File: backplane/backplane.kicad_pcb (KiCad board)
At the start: 2 copper layers, 200 x 300 mm, 117 parts, among them J1 Conn_PCB1, J10 Conn_SSR_INPUT, J11 FAN, J12 Conn_SSR_PCB2, J13 FLOW, J14 FCC_B2B, J15 AQ2, J16 AQ1, J17 O3, J18 Conn_TO_ION_AIR, J2 Conn_PCB2, J22 POWER, J23 PCB1_COMM_CONNECTOR, J24 Conn_01x14, J25 PCB1_ALARM, J26 Conn_01x12, J27 Conn_01x15, J28 PMS7003S_CONN, J3 SSR_CONTROL, J4 TO_CONTROL_BOARD, J5 Conn_SSR_POWER_SOURCE, J6 48V_SRC, J7 WS2812, J8 PURFUME, J9 SSR2, Q1 2N3904(1AM), Q2 2N3904(1AM), Q3 2N3904(1AM), Q4 SS9013_J3, SW1 SW_Push, U1 OMRON-G3MB-202P, U2 OMRON-G3MB-202P, U3 waveshare-swd-pinsocket, U4 STM32F103C8T6, U5 AMS1117-3.3, U6 74AHCT1G125, U7 SP3232EEN, Y1 O8M, Y2 O_EPSON_32.768K

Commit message: update comments,
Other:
- board text added: "add 8 pin sub connector add mount hold for sub-board"
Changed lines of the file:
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@@
   (general
     (thickness 1.6)
-    (drawings 22)
+    (drawings 23)
     (tracks 1527)
     (zones 0)
@@
     )
   )
+  (gr_text "add 8 pin sub connector\nadd mount hold for sub-board\n" (at -5.21 44.15 90) (layer F.Cu)
+    (effects (font (size 1.5 1.5) (thickness 0.3)))
+  )
   (gr_circle (center 10 285) (end 16 285) (layer Dwgs.User) (width 1))

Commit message: update PCB2 done,
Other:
- board text added: "PCB2"

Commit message: update PCB1 done,
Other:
- board text added: "PCB1"
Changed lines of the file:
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@@
   (general
     (thickness 1.6)
-    (drawings 40)
+    (drawings 57)
     (tracks 1527)
     (zones 0)
@@
     )
   )
+  (gr_text PCB1 (at 335.5 245) (layer Dwgs.User)
+    (effects (font (size 3 3) (thickness 0.5)))
+  )
+  (gr_circle (center 321.75 202.25) (end 323.5 202.25) (layer Dwgs.User) (width 0.5))
+  (gr_circle (center 353.25 146.75) (end 355 146.75) (layer Dwgs.User) (width 0.5))
+  (gr_circle (center 353.25 202.25) (end 355 202.25) (layer Dwgs.User) (width 0.5))
+  (gr_circle (center 277.75 256.25) (end 279.5 256.25) (layer Dwgs.User) (width 0.5))
+  (gr_circle (center 341.75 256.25) (end 343.5 256.25) (layer Dwgs.User) (width 0.5))
+  (gr_circle (center 237.25 122.25) (end 239 122.25) (layer Dwgs.User) (width 0.5))
+  (gr_line (start 223.5 223.5) (end 223.5 118.5) (layer Dwgs.User) (width 0.5))
+  (gr_line (start 203.5 223) (end 223.5 223) (layer Dwgs.User) (width 0.5))
+  (gr_line (start 203.5 263) (end 203.5 223) (layer Dwgs.User) (width 0.5))
+  (gr_line (start 348.5 263) (end 203.5 263) (layer Dwgs.User) (width 0.5))
+  (gr_line (start 348.5 221) (end 348.5 263) (layer Dwgs.User) (width 0.5))
+  (gr_line (start 358 221) (end 348.5 221) (layer Dwgs.User) (width 0.5))
+  (gr_line (start 358 131) (end 358 221) (layer Dwgs.User) (width 0.5))
+  (gr_line (start 348 131) (end 358 131) (layer Dwgs.User) (width 0.5))
+  (gr_line (start 348 118.5) (end 348 131) (layer Dwgs.User) (width 0.5))
+  (gr_line (start 223.5 118.5) (end 348 118.5) (layer Dwgs.User) (width 0.5))
   (gr_circle (center 392.25 111.25) (end 394 111.25) (layer Dwgs.User) (width 0.5))
   (gr_circle (center 308.75 111.25) (end 310.5 111.25) (layer Dwgs.User) (width 0.5))

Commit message: align mounting hole,
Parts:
- H1, H16, H2, H3, H4, H5, H6, H7, H8, H9: footprint MountingHole:MountingHole_3.2mm_M3_DIN965 -> MountingHole:MountingHole_3.7mm
- moved H3 22.5 mm to (195.8, 150.2)
- moved H1 1.41 mm to (79.8, 125.8)
- moved H5 1.12 mm to (195.8, 205.8)
- moved H4 0.90 mm to (105.8, 107.8)
- moved H2 0.75 mm to (189.2, 107.8)
- moved H8 0.56 mm to (105.8, 6.75)
- moved H6 0.25 mm to (189.2, 6.75)

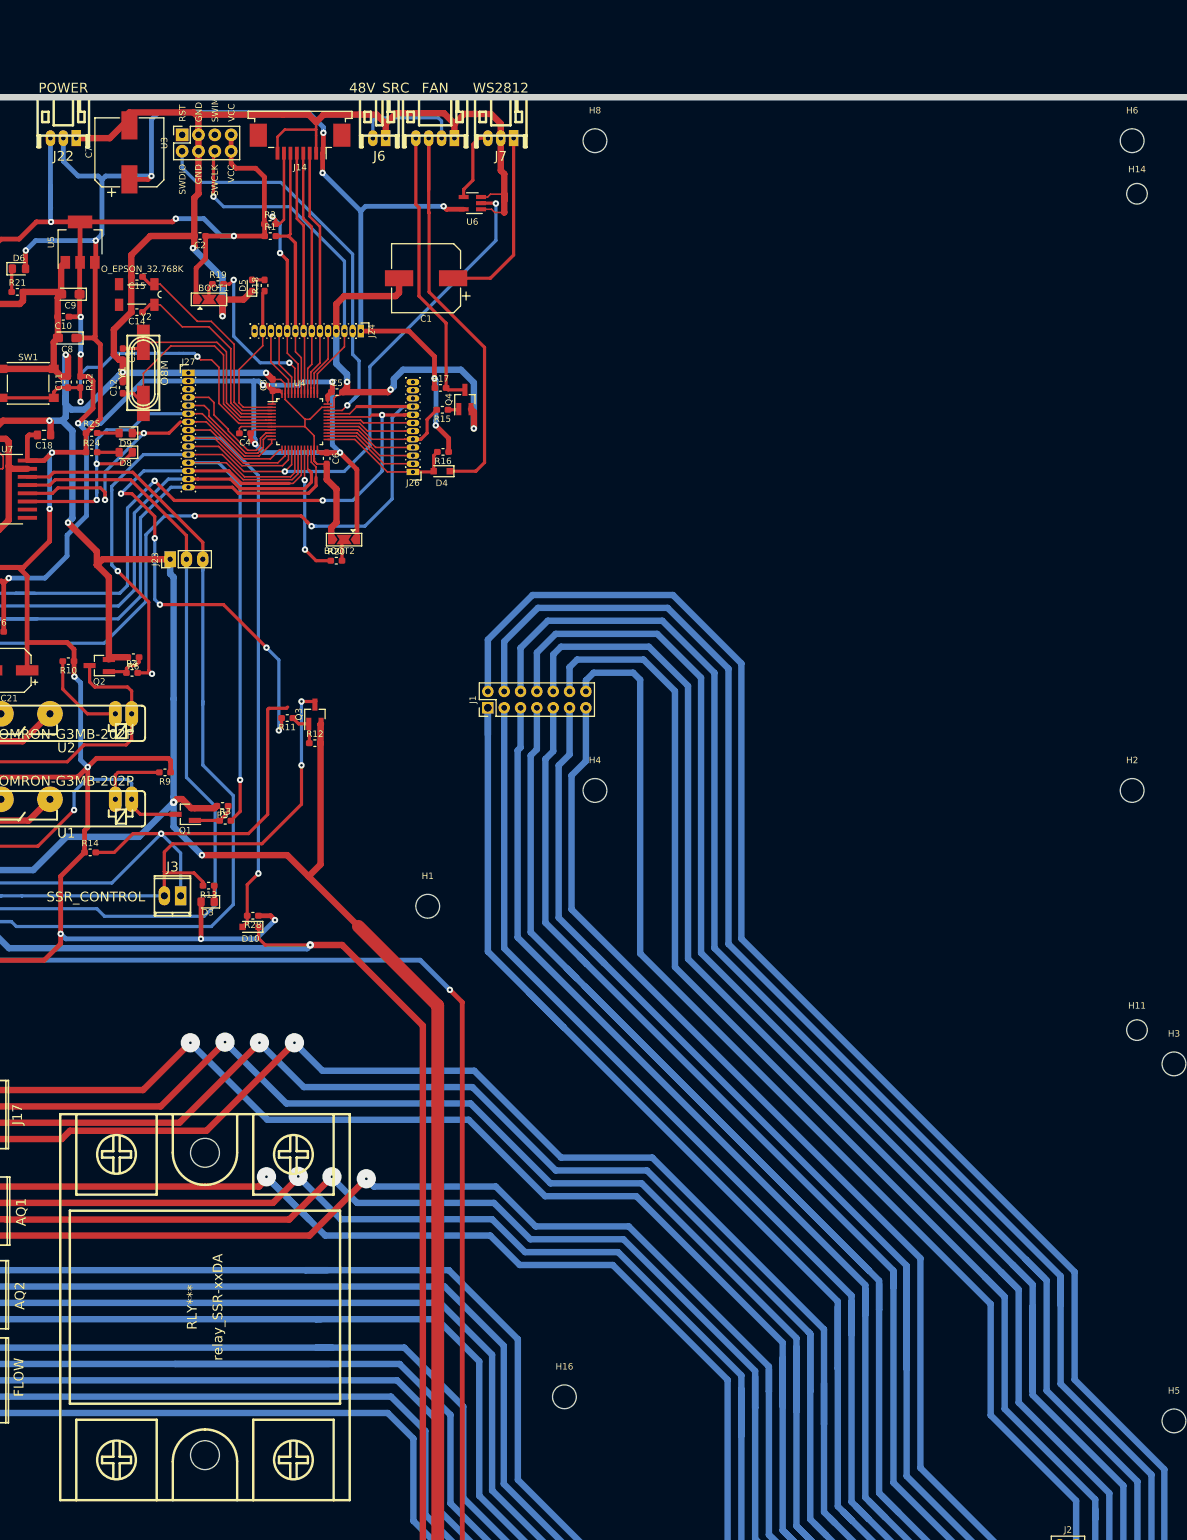
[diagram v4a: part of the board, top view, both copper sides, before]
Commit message: align mounting hole,
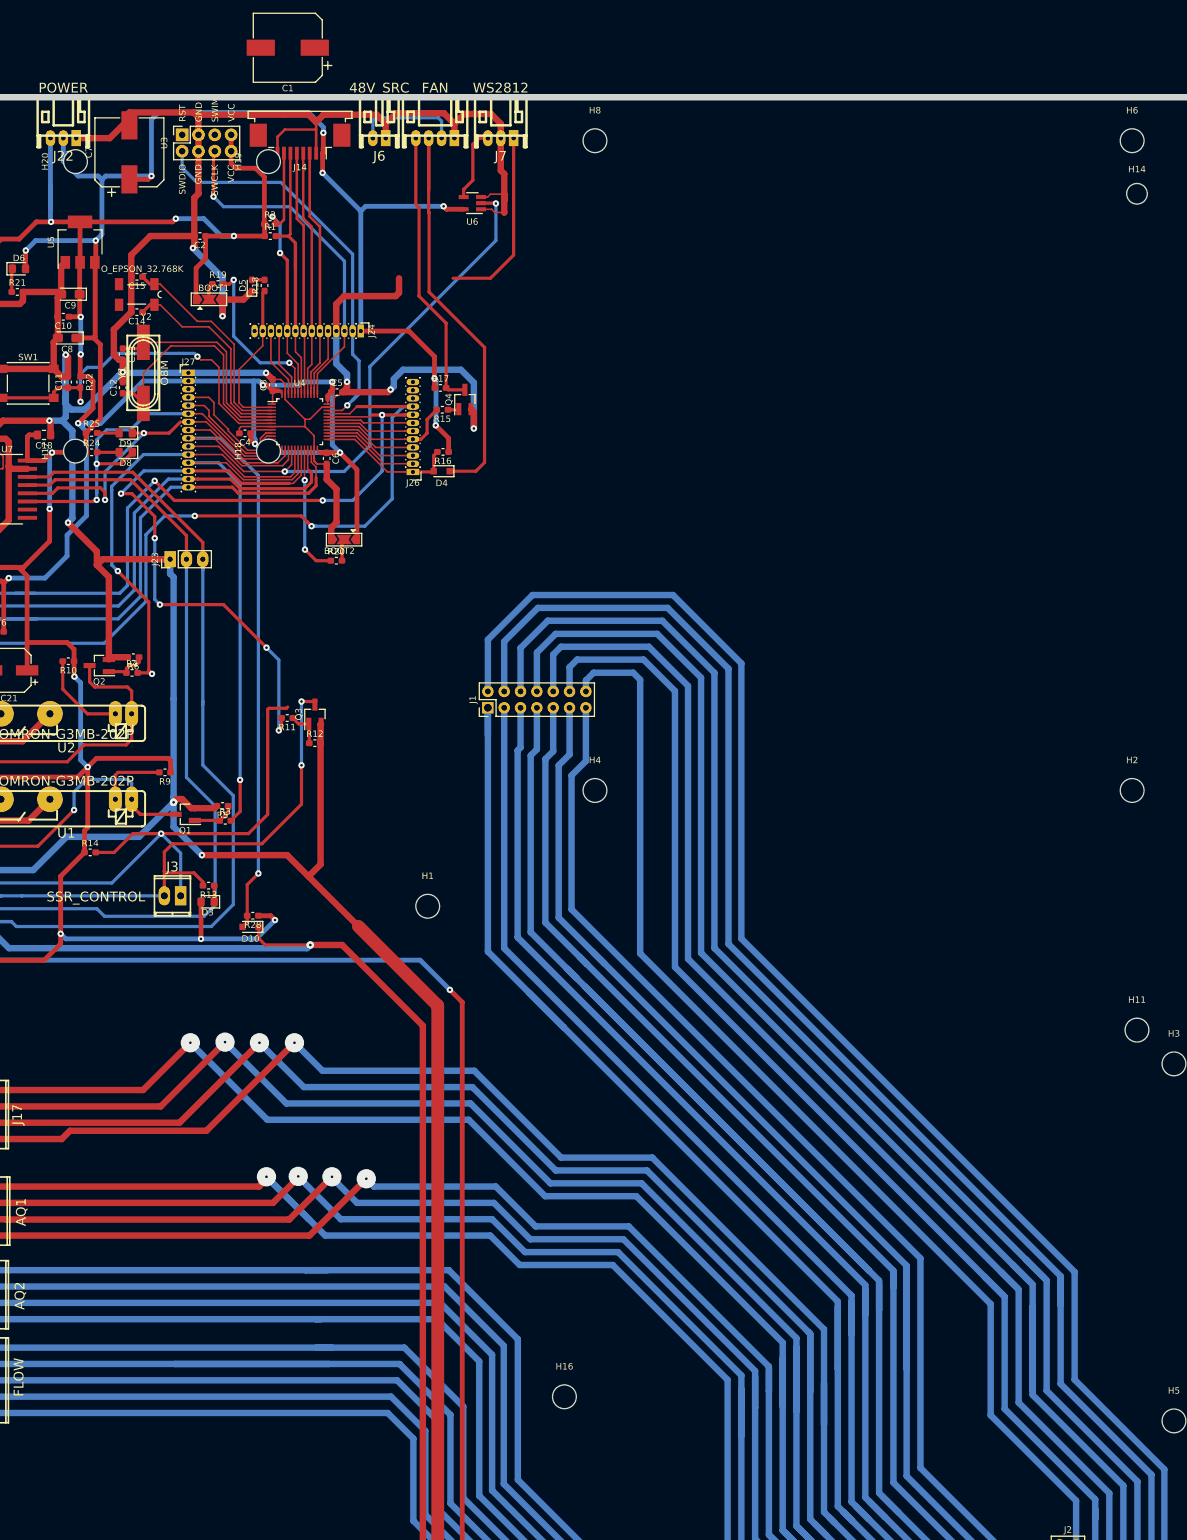
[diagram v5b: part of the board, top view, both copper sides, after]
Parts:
- removed RLY***: relay_SSR-xxDA, w_relay:relay_SSR-xxDA
- added H17: STM32_MOUNT, MountingHole:MountingHole_3.7mm, F.Cu at (25.0, 55.0)
- added H18: STM32_MOUNT, MountingHole:MountingHole_3.7mm, F.Cu at (55.0, 55.0)
- added H19: STM32_MOUNT, MountingHole:MountingHole_3.7mm, F.Cu at (55.0, 10.0)
- added H20: STM32_MOUNT, MountingHole:MountingHole_3.7mm, F.Cu at (25.0, 10.0)
- H11: footprint MountingHole:MountingHole_3.2mm_M3_DIN965 -> MountingHole:MountingHole_3.7mm
- moved C1 41.8 mm to (58.0, -7.70)
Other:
- board text added: "EXPAND BOARD"

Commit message: update,
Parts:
- moved J4 90.0 mm to (6.28, 37.1)
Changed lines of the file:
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@@
   )
   (module footprint-lib:s8b-ph-kl (layer F.Cu)
-    (at 6.283501 127.13 270)
+    (at 6.283501 37.13 270)
     (descr "JST PH series connector, S8B-PH-KL")
     (clearance 0.3)

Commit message: update,
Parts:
- moved C1 25.3 mm to (49.2, 16.0)
- moved J22 12.0 mm to (35.1, 6.36)
- moved D7 7.62 mm to (2.76, 24.9), turned to 90 degrees
- moved C7 7.58 mm to (34.8, 16.0), turned to 0 degrees
- moved D6 7.26 mm to (9.17, 24.9), turned to 90 degrees
- moved R23 6.86 mm to (5.36, 25.1), turned to 90 degrees
- moved R21 6.62 mm to (11.8, 25.1), turned to 90 degrees
- moved C15 5.59 mm to (32.0, 22.9)
- moved Y2 5.59 mm to (32.0, 25.7)
- moved C14 5.59 mm to (32.0, 28.4)
- moved U5 3.90 mm to (23.5, 19.3)
- moved R1 3.79 mm to (54.1, 25.2)
- moved R2 3.79 mm to (54.0, 23.3)
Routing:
- net SSR-25-DA_P: track 98.4 -> 201.2 mm, vias 1 -> 4
- net SSR-25-DA_N: track 94.2 -> 196.3 mm, vias 2 -> 4
- net PCB1_ALARM_COM: track 232.0 -> 333.2 mm, vias 1 -> 2
- net IONAIR_RX: track 133.8 -> 70.4 mm, vias 0 -> 2
- net IONAIR_TX: track 144.1 -> 89.4 mm, vias 0 -> 2
- net VWS2812: track 29.1 -> 60.7 mm, vias 0 -> 3
- net GND: track 851.8 -> 835.2 mm, vias 12 -> 14
- net +3V3: track 290.0 -> 298.5 mm, vias 11 -> 10
- net +5V: track 683.3 -> 674.9 mm, vias 16 -> 17
- net /stm32_board/STM32_CORE/PC15: track 32.5 -> 39.9 mm
- net B2B_UART_RX: track 42.4 -> 47.5 mm
- net /stm32_board/STM32_CORE/PC14: track 36.3 -> 41.3 mm
- net IONAIR-TTL-RX: track 53.7 -> 58.3 mm
- net IONAIR-TTL-TX: track 60.2 -> 64.7 mm
- net B2B_UART_TX: track 44.2 -> 41.3 mm
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
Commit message: update,
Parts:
- moved J14 6.50 mm to (66.4, 6.89)
- moved J11 6.50 mm to (87.4, 6.36)
- moved J6 6.50 mm to (78.7, 6.36)
- moved J7 6.50 mm to (97.6, 6.36)
- moved U6 6.50 mm to (93.2, 16.5)
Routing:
- net +5V: track 674.9 -> 689.6 mm
- net STM32_WS2812_OUTPUT: track 83.4 -> 94.6 mm
- net GND: track 835.2 -> 824.9 mm, vias 14 -> 15
- net B2B_UART_TX: track 41.3 -> 50.1 mm
- net /stm32_board/FAN_RPM: track 68.1 -> 74.6 mm
- net SPI1_MISO: track 38.2 -> 42.6 mm
- net VWS2812: track 60.7 -> 64.3 mm
- net SPI1_SCK: track 38.6 -> 41.3 mm
- net SPI1_MOSI: track 37.9 -> 40.2 mm
- net /stm32_board/FAN_PWM_OUTPUT: track 43.8 -> 46.1 mm
- net B2B_UART_RX: track 47.5 -> 48.9 mm
